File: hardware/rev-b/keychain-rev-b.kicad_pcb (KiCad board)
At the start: 4 copper layers, 30 x 46 mm, 57 parts, among them J1 USB-C, J2 OLED 0.96" I2C, J3 SWD, M1 вибромотор 0820, Q1 AO3401A, Q2 AO3401A, Q3 AO3400A, Q4 AO3400A, SW1 B3U-3100P, U1 MDBT50Q-1MV2, U2 MCP73832-2, U3 USBLC6-2SC6, U4 LIS3DH, U5 LTR-303ALS-01, U6 SPH0641LM4H-1

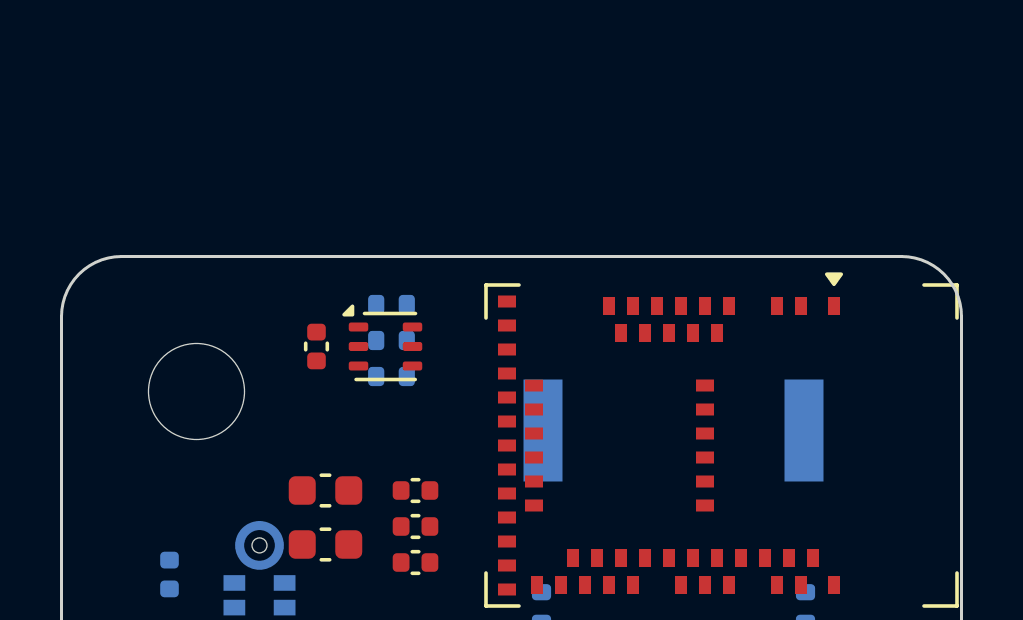
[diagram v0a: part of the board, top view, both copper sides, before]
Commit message: Плата rev B: ушко для кольца по центру сверху, перебор порядка шин питания
Отверстие под кольцо вынесено из угла в отдельный выступ над верхним
краем, угол освободился под разводку. Маршрутизатор питания кэширует
маску краёв и пробует разные порядки цепей.

Co-Authored-By: Claude Opus 5.5 <noreply@anthropic.com>
Claude-Session: https://claude.ai/code/session_01RQ7GfaTDyVK1Dcdo3sKM8F
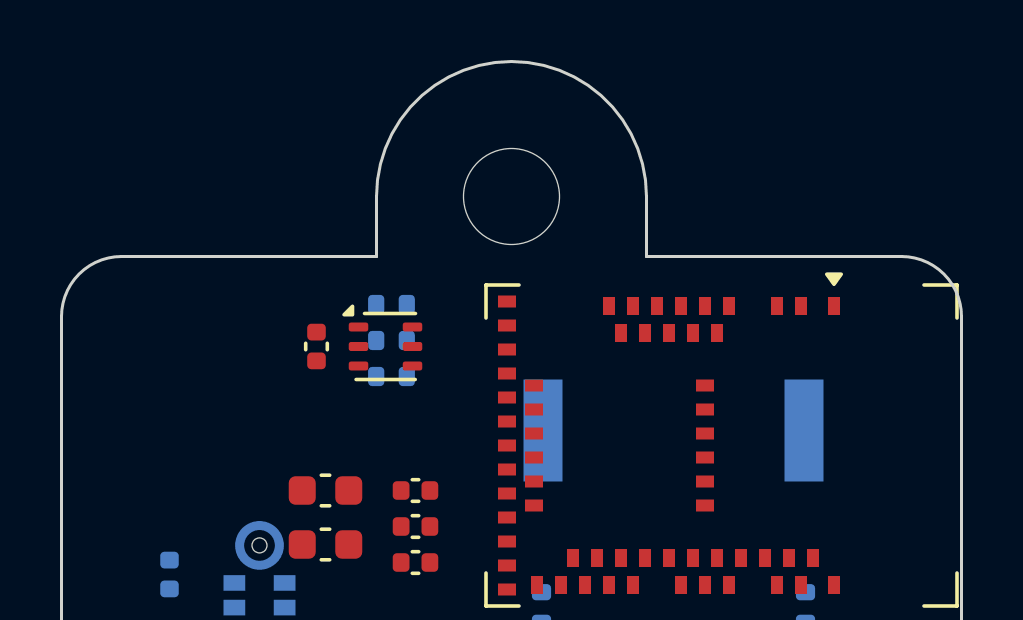
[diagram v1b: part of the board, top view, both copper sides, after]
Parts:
- moved H1 12.3 mm to (15.0, -2.00)
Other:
- board size 30 x 46 mm -> 30 x 52.5 mm

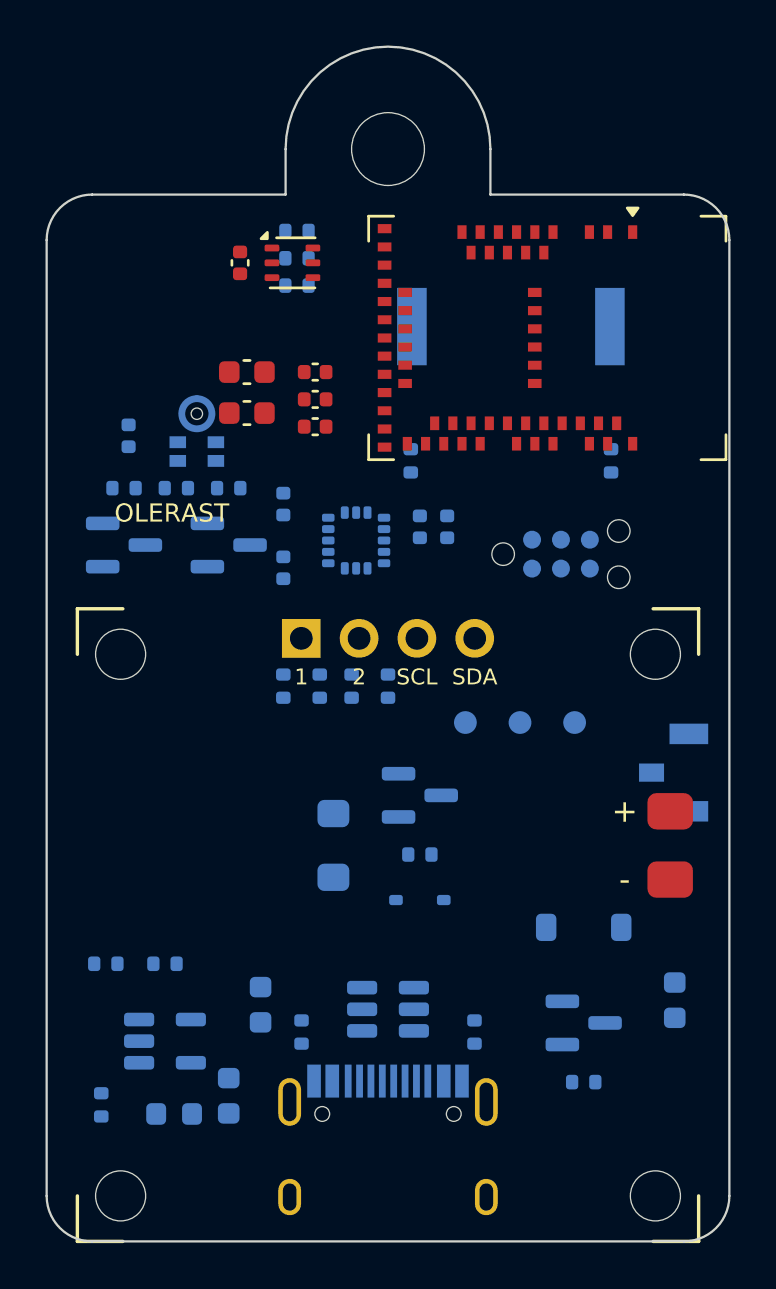
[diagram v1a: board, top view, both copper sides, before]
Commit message: Разводка: земля в задаче роутера — плоскостью, а не запретными зонами
Отводы земли как запретные зоны перекрывали соседние сигнальные
площадки. Плоскость GND в L2 роутер считает подключённой через
переходные. Исправлена порча координат сохранённых отводов.

Co-Authored-By: Claude Opus 5.5 <noreply@anthropic.com>
Claude-Session: https://claude.ai/code/session_01RQ7GfaTDyVK1Dcdo3sKM8F
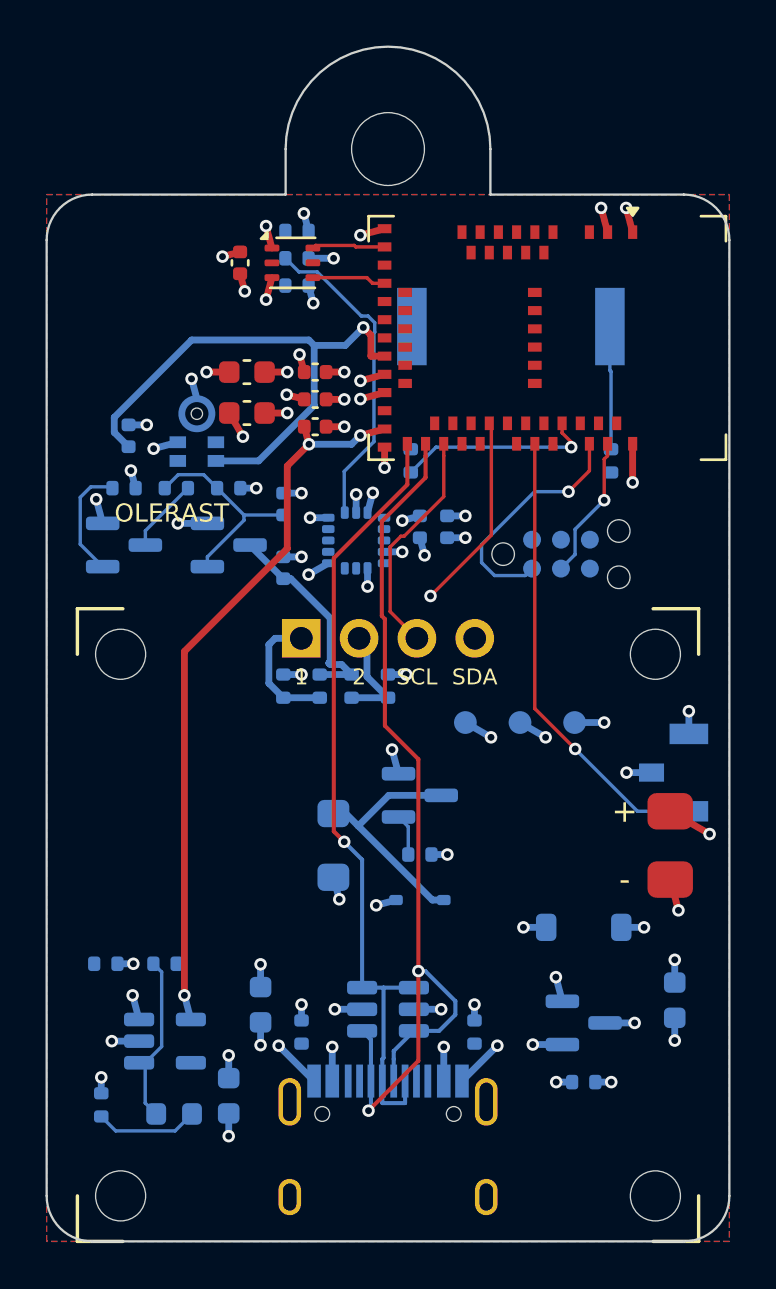
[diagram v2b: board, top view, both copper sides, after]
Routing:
- net VBUS: track 0.00 -> 90.1 mm, vias 0 -> 11
- net VSYS: track 0.00 -> 82.1 mm, vias 0 -> 12
- net VDD: track 0.00 -> 75.2 mm, vias 0 -> 14
- net VBAT: track 0.00 -> 67.4 mm, vias 0 -> 4
- net USB_DP: track 0.00 -> 42.8 mm, vias 0 -> 2
- net GND: track 0.00 -> 42.4 mm, vias 0 -> 42
- net USB_DN: track 0.00 -> 35.1 mm, vias 0 -> 1
- net MIC_PWR: track 0.00 -> 24.3 mm, vias 0 -> 1
- net BTN: track 0.00 -> 20.3 mm, vias 0 -> 1
- net SENS_SDA: track 0.00 -> 17.2 mm
- net DISP_EN: track 0.00 -> 13.8 mm, vias 0 -> 1
- net SWDIO: track 0.00 -> 10.6 mm, vias 0 -> 1
- net VIB_N: track 0.00 -> 10.6 mm
- net DISP_SCL: track 0.00 -> 10.1 mm
- net DISP_VCC: track 0.00 -> 9.47 mm
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- added copper zone on B.Cu, net GND
- added copper zone on F.Cu, net GND
- added copper zone on In1.Cu, net GND
- added copper zone on In2.Cu, net GND

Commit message: Плата rev B разведена: 0 несоединённых, 0 ошибок DRC
Сигналы пущены и во внутренний слой L3 рядом с шинами питания (опора —
сплошная земля L2). Шины питания сужены до 0.4/0.3 мм. Раскладка
переходных детерминирована и учитывает зазоры классов. Остаток после
Freerouting прокладывает свой трассировщик (fixroute.py) по слоям
L1/L3/L4 с переходными; обрезки и висящие переходные убираются.
Питание микрофона — обычной дорожкой. Края платы — запретной полосой.

Co-Authored-By: Claude Opus 5.5 <noreply@anthropic.com>
Claude-Session: https://claude.ai/code/session_01RQ7GfaTDyVK1Dcdo3sKM8F
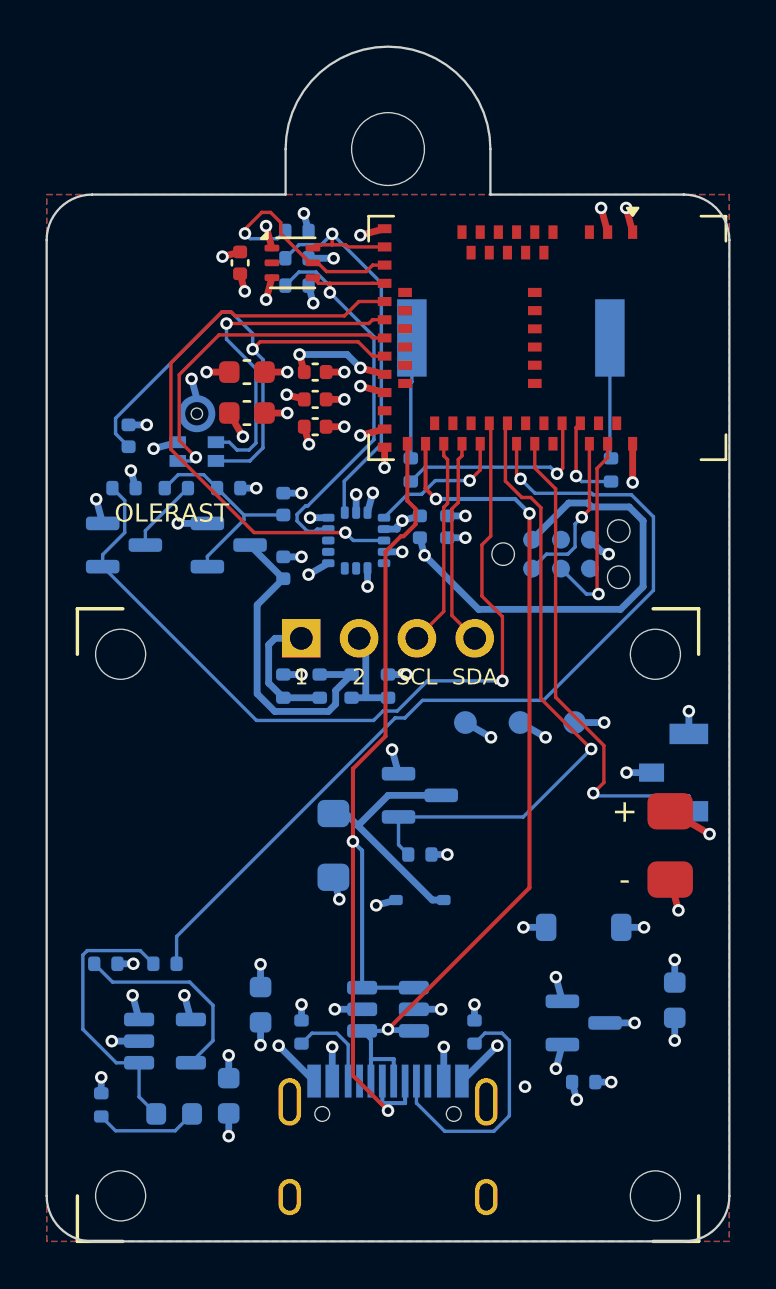
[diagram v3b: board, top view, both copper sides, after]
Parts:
- moved BZ1 0.50 mm to (20.4, 6.30)
- moved R13 0.40 mm to (16.0, 12.1)
- moved R14 0.40 mm to (24.8, 12.1)
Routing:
- net VDD: track 75.2 -> 142.9 mm
- net VSYS: track 82.1 -> 129.9 mm
- net CHG_IO: track 0.00 -> 39.8 mm, vias 0 -> 1
- net VIB_EN: track 1.83 -> 27.7 mm, vias 0 -> 1
- net ACC_INT1: track 0.00 -> 25.5 mm, vias 0 -> 1
- net DISP_EN: track 13.8 -> 37.0 mm
- net VBAT: track 67.4 -> 48.3 mm
- net SENS_SCL: track 3.25 -> 20.3 mm, vias 0 -> 1
- net PDM_CLK: track 0.00 -> 14.8 mm, vias 0 -> 1
- net PDM_DATA: track 0.00 -> 14.6 mm, vias 0 -> 1
- net CC1: track 0.00 -> 11.0 mm
- net ALS_INT: track 0.00 -> 10.1 mm, vias 0 -> 1
- net DISP_SDA: track 0.00 -> 9.15 mm
- net PROG: track 0.00 -> 8.90 mm
- net USB_DN: track 35.1 -> 43.4 mm, vias 1 -> 2
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
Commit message: Плата rev B: исправления перед заказом, разведена заново
- «100k» в BOM был с номером LCSC C25086 — это не 100 кОм (у LCSC/JLCPCB
  1 Ом): на R6 закоротило бы VBUS, на R7/R9/R15 не работали бы экран и вибро.
  Теперь C25741 (0402WGF1003TCE, базовая).
- R6 10 кОм: после отключения USB Q1 открывается за ~15 мс, а не ~130 мс
  (VSYS падал до 2.5 В), утечка горячего Шоттки не поднимает VBUS.
- C11 между затвором и стоком Q2: бросок тока экрана ~0.14 А вместо
  0.6–1.3 А, VSYS не ниже 3.64 В (SPICE).
- R20 100 кОм с CHG_IO на землю: «1» статуса заряда 2.8–3.4 В вместо 3.8 В
  (выше VDD + 0.3 В).
- Ячейка на 1.4 мм ниже: не налезает на штыревой разъём экрана.
- README: модуль экрана с LDO, повороты деталей оборота в предпросмотре
  JLCPCB, зазоры ячейки и USB-C, итог проверки.

DRC: 0 ошибок, 0 несоединённых (предупреждение шелкографии — прежнее);
схема сверена с netlist.py, расхождений 0.

Co-Authored-By: Claude Opus 5.5 <noreply@anthropic.com>
Claude-Session: https://claude.ai/code/session_01RQ7GfaTDyVK1Dcdo3sKM8F
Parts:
- added R20: 100k, Resistor_SMD:R_0402_1005Metric, B.Cu at (7.60, 33.8)
- R6: value 100k -> 10k
- moved BT1 1.40 mm to (15.0, 33.5)
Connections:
- C11 pad 2: VSYS -> DISP_VCC
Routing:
- net VDD: track 142.9 -> 131.0 mm
- net CC1: track 11.0 -> 4.26 mm
- net USB_DP: track 40.0 -> 34.0 mm, vias 3 -> 1
- net VSYS: track 129.9 -> 124.7 mm, vias 12 -> 11
- net VIB_EN: track 27.7 -> 22.9 mm
- net DISP_G: track 9.12 -> 13.8 mm
- net DISP_VCC: track 14.5 -> 19.0 mm, vias 0 -> 3
- net PDM_DATA: track 14.6 -> 19.0 mm, vias 1 -> 2
- net GND: track 48.8 -> 44.4 mm
- net PDM_CLK: track 14.8 -> 11.0 mm
- net CHG_IO: track 39.8 -> 36.6 mm
- net SWDIO: track 7.08 -> 10.2 mm
- net SENS_SCL: track 20.3 -> 23.4 mm
- net USB_DN: track 43.4 -> 46.1 mm, vias 2 -> 1
- net SWDCLK: track 8.94 -> 6.33 mm
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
